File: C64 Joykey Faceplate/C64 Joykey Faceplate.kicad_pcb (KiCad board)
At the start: 2 copper layers, 99.7 x 74.9 mm, 4 parts, among them M1 Mounting, M2 Mounting, M3 Mounting, M4 Mounting

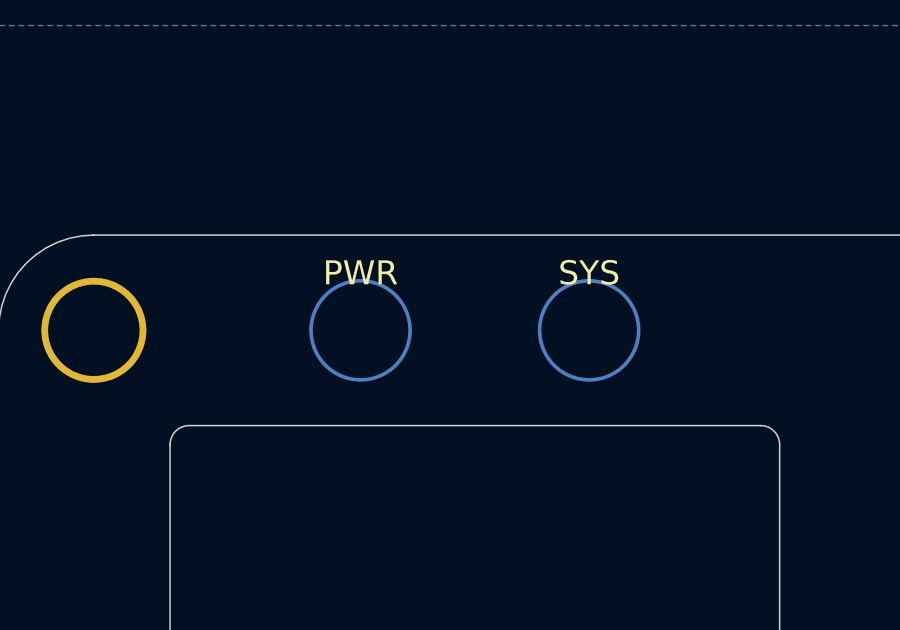
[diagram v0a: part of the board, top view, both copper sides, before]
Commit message: Tweaked faceplate
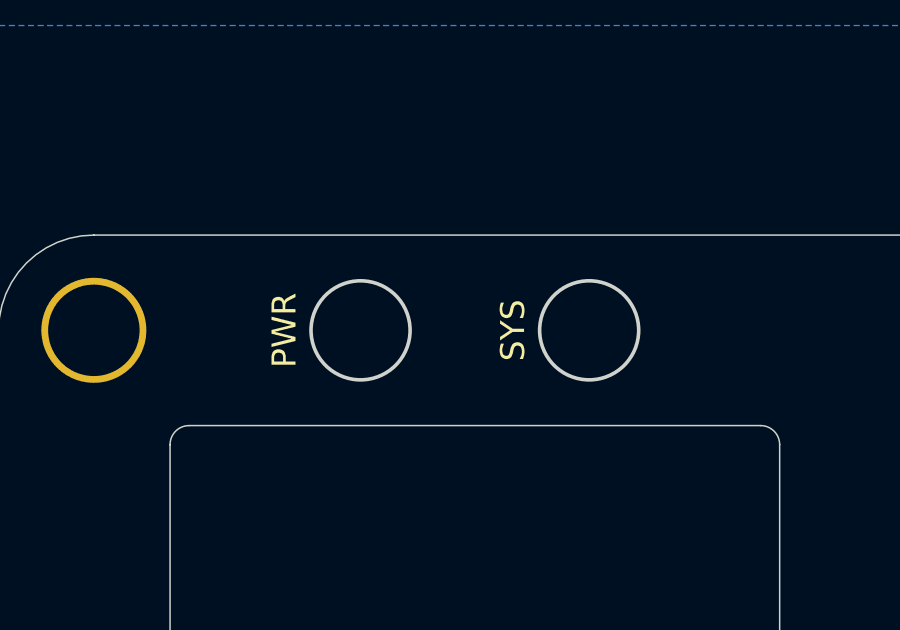
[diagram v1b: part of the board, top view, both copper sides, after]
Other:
- outline, holes or cut-outs redrawn
- rule pad_to_mask_clearance: 0.051 -> 0
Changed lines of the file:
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@@
-(kicad_pcb (version 20171130) (host pcbnew "(5.1.5)-3")
+(kicad_pcb (version 20171130) (host pcbnew "(5.1.8)-1")
   (general
     (thickness 1.6)
@@
     (pad_size 1.524 1.524)
     (pad_drill 0.762)
-    (pad_to_mask_clearance 0.051)
-    (solder_mask_min_width 0.25)
+    (pad_to_mask_clearance 0)
     (aux_axis_origin 0 0)
     (visible_elements 7FFFFFFF)
@@
       (effects (font (size 1 1) (thickness 0.15)))
     )
+    (fp_circle (center 0 0) (end 2.6 0) (layer F.CrtYd) (width 0.05))
     (fp_circle (center 0 0) (end 2 0.8) (layer F.Fab) (width 0.1))
-    (fp_circle (center 0 0) (end 2.6 0) (layer F.CrtYd) (width 0.05))
     (pad 1 thru_hole circle (at 0 0) (size 3.5 3.5) (drill 3.048) (layers *.Cu *.Mask)
       (net 1 "Net-(M1-Pad1)") (solder_mask_margin 0.8))
@@
       (effects (font (size 1 1) (thickness 0.15)))
     )
+    (fp_circle (center 0 0) (end 2 0.8) (layer F.Fab) (width 0.1))
     (fp_circle (center 0 0) (end 2.6 0) (layer F.CrtYd) (width 0.05))
-    (fp_circle (center 0 0) (end 2 0.8) (layer F.Fab) (width 0.1))
     (pad 1 thru_hole circle (at 0 0) (size 3.5 3.5) (drill 3.048) (layers *.Cu *.Mask)
       (net 1 "Net-(M1-Pad1)") (solder_mask_margin 0.8))
@@
       (effects (font (size 1 1) (thickness 0.15)))
     )
+    (fp_circle (center 0 0) (end 2.6 0) (layer F.CrtYd) (width 0.05))
     (fp_circle (center 0 0) (end 2 0.8) (layer F.Fab) (width 0.1))
-    (fp_circle (center 0 0) (end 2.6 0) (layer F.CrtYd) (width 0.05))
     (pad 1 thru_hole circle (at 0 0) (size 3.5 3.5) (drill 3.048) (layers *.Cu *.Mask)
       (net 1 "Net-(M1-Pad1)") (solder_mask_margin 0.8))
@@
       (effects (font (size 1 1) (thickness 0.15)))
     )
+    (fp_circle (center 0 0) (end 2 0.8) (layer F.Fab) (width 0.1))
     (fp_circle (center 0 0) (end 2.6 0) (layer F.CrtYd) (width 0.05))
-    (fp_circle (center 0 0) (end 2 0.8) (layer F.Fab) (width 0.1))
     (pad 1 thru_hole circle (at 0 0) (size 3.5 3.5) (drill 3.048) (layers *.Cu *.Mask)
       (net 1 "Net-(M1-Pad1)") (solder_mask_margin 0.8))
@@
     (effects (font (size 1 1) (thickness 0.15)))
   )
-  (gr_text SYS (at 160.655 83.82) (layer F.SilkS)
+  (gr_text SYS (at 158.115 85.725 90) (layer F.SilkS)
     (effects (font (size 0.8 0.8) (thickness 0.1)))
   )
-  (gr_text PWR (at 153.035 83.82) (layer F.SilkS)
+  (gr_text PWR (at 150.495 85.725 90) (layer F.SilkS)
     (effects (font (size 0.8 0.8) (thickness 0.1)))
   )
-  (gr_circle (center 160.655 85.725) (end 162.306 85.725) (layer B.Cu) (width 0.12))
-  (gr_circle (center 153.035 85.725) (end 154.686 85.725) (layer B.Cu) (width 0.12))
+  (gr_circle (center 160.655 85.725) (end 162.306 85.725) (layer Edge.Cuts) (width 0.12))
+  (gr_circle (center 153.035 85.725) (end 154.686 85.725) (layer Edge.Cuts) (width 0.12))
   (gr_circle (center 160.655 85.725) (end 161.925 85.725) (layer B.Mask) (width 2.5))
   (gr_circle (center 153.035 85.725) (end 154.305 85.725) (layer B.Mask) (width 2.5))
